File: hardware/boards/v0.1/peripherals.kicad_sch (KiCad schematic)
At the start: 7 parts, among them IC2 DA7280-00FVC, U21 LSM6DS3

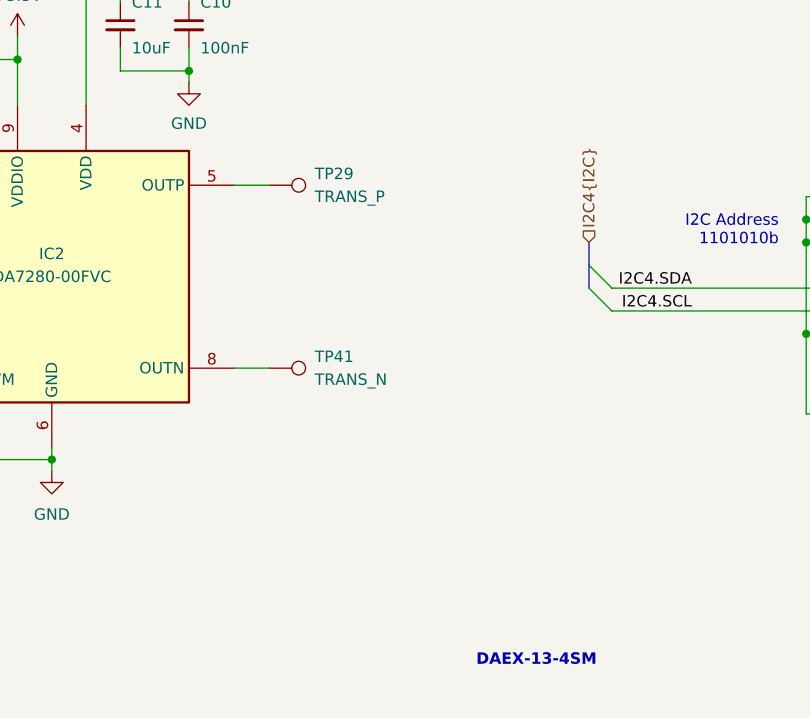
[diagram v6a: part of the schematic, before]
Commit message: feat: switch FM transmitter to I2S
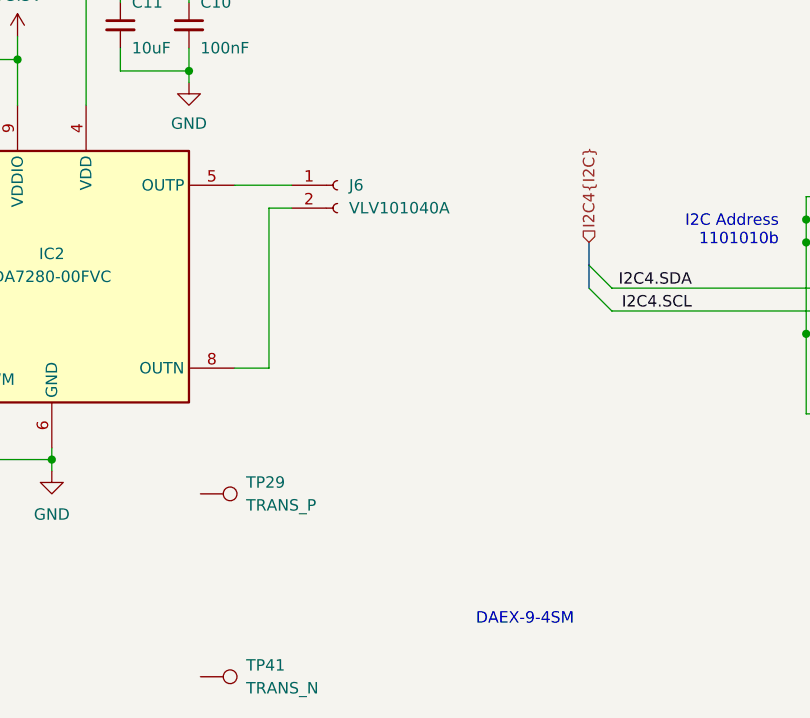
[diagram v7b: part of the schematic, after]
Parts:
- added J6: VLV101040A, pocket_synth:825-22-002-10-001101, symbol Connector:Conn_01x02_Socket
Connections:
- net at TP41.1: no longer IC2.8 (OUTN)
- net at IC2.5 (OUTP): now also J6.1 (Pin_1); no longer TP29.1
- new net: IC2.8 (OUTN), J6.2 (Pin_2)
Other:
- note added: "DAEX-9-4SM"
- note removed: "DAEX-13-4SM"
- moved on the sheet: TP29, TP41
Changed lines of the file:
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@@
 	(generator_version "9.0")
 	(paper "A4")
-	(text "DAEX-13-4SM"
+	(text "DAEX-9-4SM"
 		(exclude_from_sim no)
-		(at 116.078 103.632 0)
+		(at 114.808 99.06 0)
 		(effects
 			(font
 				(size 1.27 1.27)
-				(thickness 0.254)
-				(bold yes)
 			)
 		)
@@
 	(wire
 		(pts
+			(xy 86.36 53.34) (xy 88.9 53.34)
+		)
+		(stroke
+			(width 0)
+			(type default)
+		)
+	)
+	(wire
+		(pts
 			(xy 24.13 53.34) (xy 41.91 53.34)
 		)
@@
 	(wire
 		(pts
+			(xy 86.36 71.12) (xy 86.36 53.34)
+		)
+		(stroke
+			(width 0)
+			(type default)
+		)
+	)
+	(wire
+		(pts
 			(xy 147.32 64.77) (xy 124.46 64.77)
 		)
@@
 	(wire
 		(pts
-			(xy 82.55 50.8) (xy 86.36 50.8)
+			(xy 82.55 50.8) (xy 88.9 50.8)
 		)
 		(stroke
@@
 	(symbol
 		(lib_id "Connector:TestPoint")
-		(at 86.36 71.12 270)
+		(at 78.74 105.41 270)
 		(unit 1)
 		(exclude_from_sim no)
@@
 		(fields_autoplaced yes)
 		(property "Reference" "TP41"
-			(at 91.44 69.8499 90)
+			(at 83.82 104.1399 90)
 			(effects
 				(font
@@
 		)
 		(property "Value" "TRANS_N"
-			(at 91.44 72.3899 90)
+			(at 83.82 106.6799 90)
 			(effects
 				(font
@@
 		)
 		(property "Footprint" "TestPoint:TestPoint_Pad_D2.5mm"
-			(at 86.36 76.2 0)
+			(at 78.74 110.49 0)
 			(effects
 				(font
@@
 		)
 		(property "Datasheet" "~"
-			(at 86.36 76.2 0)
+			(at 78.74 110.49 0)
 			(effects
 				(font
@@
 		)
 		(property "Description" "test point"
-			(at 86.36 71.12 0)
+			(at 78.74 105.41 0)
 			(effects
 				(font
@@
 	)
 	(symbol
+		(lib_id "Connector:Conn_01x02_Socket")
+		(at 93.98 50.8 0)
+		(unit 1)
+		(exclude_from_sim no)
+		(in_bom yes)
+		(on_board yes)
+		(dnp no)
+		(fields_autoplaced yes)
+		(property "Reference" "J6"
+			(at 95.25 50.7999 0)
+			(effects
+				(font
+					(size 1.27 1.27)
+				)
+				(justify left)
+			)
+		)
+		(property "Value" "VLV101040A"
+			(at 95.25 53.3399 0)
+			(effects
+				(font
+					(size 1.27 1.27)
+				)
+				(justify left)
+			)
+		)
+		(property "Footprint" "pocket_synth:825-22-002-10-001101"
+			(at 93.98 50.8 0)
+			(effects
+				(font
+					(size 1.27 1.27)
+				)
+				(hide yes)
+			)
+		)
+		(property "Datasheet" "~"
+			(at 93.98 50.8 0)
+			(effects
+				(font
+					(size 1.27 1.27)
+				)
+				(hide yes)
+			)
+		)
+		(property "Description" "Generic connector, single row, 01x02, script generated"
+			(at 93.98 50.8 0)
+			(effects
+				(font
+					(size 1.27 1.27)
+				)
+				(hide yes)
+			)
+		)
+		(pin "2"
+		)
+		(pin "1"
+		)
+		(instances
+			(project ""
+				(path "/485383b8-00f4-4405-b270-de249939cff4/f91e71c7-727a-4ef4-a387-8ca9d7b49c20"
+					(reference "J6")
+					(unit 1)
+				)
+			)
+		)
+	)
+	(symbol
 		(lib_id "Connector:TestPoint")
-		(at 86.36 50.8 270)
+		(at 78.74 85.09 270)
 		(unit 1)
 		(exclude_from_sim no)
@@
 		(fields_autoplaced yes)
 		(property "Reference" "TP29"
-			(at 91.44 49.5299 90)
+			(at 83.82 83.8199 90)
 			(effects
 				(font
@@
 		)
 		(property "Value" "TRANS_P"
-			(at 91.44 52.0699 90)
+			(at 83.82 86.3599 90)
 			(effects
 				(font
@@
 		)
 		(property "Footprint" "TestPoint:TestPoint_Pad_D2.5mm"
-			(at 86.36 55.88 0)
+			(at 78.74 90.17 0)
 			(effects
 				(font
@@
 		)
 		(property "Datasheet" "~"
-			(at 86.36 55.88 0)
+			(at 78.74 90.17 0)
 			(effects
 				(font
@@
 		)
 		(property "Description" "test point"
-			(at 86.36 50.8 0)
-			(effects
-				(font
+			(at 78.74 85.09 0)
+			(effects
+				(font

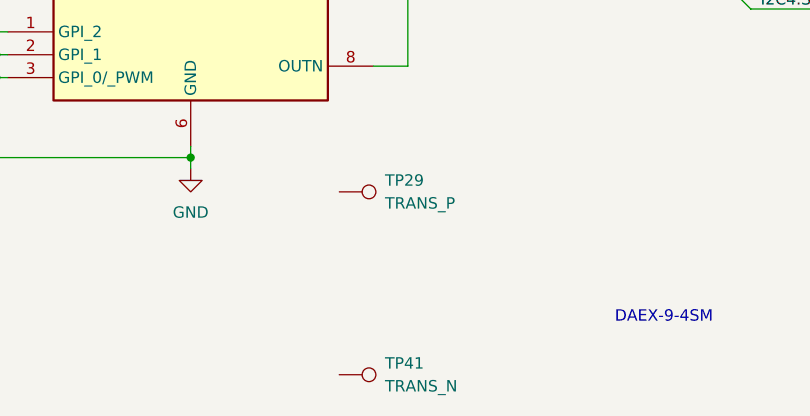
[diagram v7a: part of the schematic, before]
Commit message: feat: add FM reset pins, add fiducials
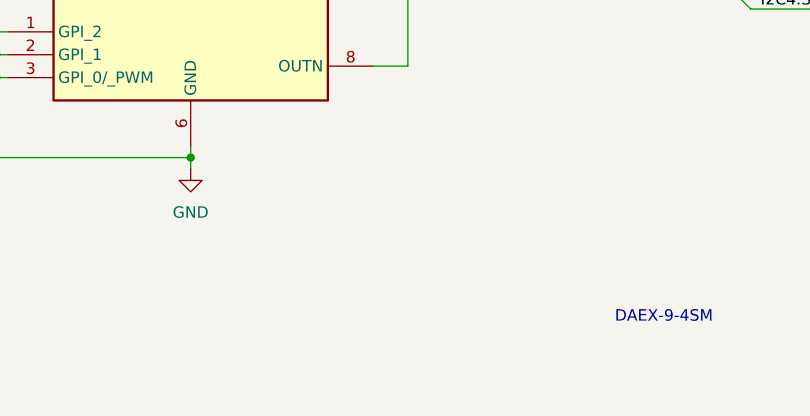
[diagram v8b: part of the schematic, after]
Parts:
- removed TP29: TRANS_P, TestPoint:TestPoint_Pad_D2.5mm, symbol Connector:TestPoint
- removed TP41: TRANS_N, TestPoint:TestPoint_Pad_D2.5mm, symbol Connector:TestPoint
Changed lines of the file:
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@@
-	)
-	(symbol
-		(lib_id "Connector:TestPoint")
-		(at 78.74 105.41 270)
-		(unit 1)
-		(exclude_from_sim no)
-		(in_bom yes)
-		(on_board yes)
-		(dnp no)
-		(fields_autoplaced yes)
-		(property "Reference" "TP41"
-			(at 83.82 104.1399 90)
-			(effects
-				(font
-					(size 1.27 1.27)
-				)
-				(justify left)
-			)
-		)
-		(property "Value" "TRANS_N"
-			(at 83.82 106.6799 90)
-			(effects
-				(font
-					(size 1.27 1.27)
-				)
-				(justify left)
-			)
-		)
-		(property "Footprint" "TestPoint:TestPoint_Pad_D2.5mm"
-			(at 78.74 110.49 0)
-			(effects
-				(font
-					(size 1.27 1.27)
-				)
-				(hide yes)
-			)
-		)
-		(property "Datasheet" "~"
-			(at 78.74 110.49 0)
-			(effects
-				(font
-					(size 1.27 1.27)
-				)
-				(hide yes)
-			)
-		)
-		(property "Description" "test point"
-			(at 78.74 105.41 0)
-			(effects
-				(font
-					(size 1.27 1.27)
-				)
-				(hide yes)
-			)
-		)
-		(pin "1"
-		)
-		(instances
-			(project "pocket_synth"
-				(path "/485383b8-00f4-4405-b270-de249939cff4/f91e71c7-727a-4ef4-a387-8ca9d7b49c20"
-					(reference "TP41")
-					(unit 1)
-				)
-			)
-		)
 	)
 	(symbol
@@
 					(unit 1)
 				)
-			)
-		)
-	)
-	(symbol
-		(lib_id "Connector:TestPoint")
-		(at 78.74 85.09 270)
-		(unit 1)
-		(exclude_from_sim no)
-		(in_bom yes)
-		(on_board yes)
-		(dnp no)
-		(fields_autoplaced yes)
-		(property "Reference" "TP29"
-			(at 83.82 83.8199 90)
-			(effects
-				(font
-					(size 1.27 1.27)
-				)
-				(justify left)
-			)
-		)
-		(property "Value" "TRANS_P"
-			(at 83.82 86.3599 90)
-			(effects
-				(font
-					(size 1.27 1.27)
-				)
-				(justify left)
-			)
-		)
-		(property "Footprint" "TestPoint:TestPoint_Pad_D2.5mm"
-			(at 78.74 90.17 0)
-			(effects
-				(font
-					(size 1.27 1.27)
-				)
-				(hide yes)
-			)
-		)
-		(property "Datasheet" "~"
-			(at 78.74 90.17 0)
-			(effects
-				(font
-					(size 1.27 1.27)
-				)
-				(hide yes)
-			)
-		)
-		(property "Description" "test point"
-			(at 78.74 85.09 0)
-			(effects
-				(font
-					(size 1.27 1.27)
-				)
-				(hide yes)
-			)
-		)
-		(pin "1"
-		)
-		(instances
-			(project ""
-				(path "/485383b8-00f4-4405-b270-de249939cff4/f91e71c7-727a-4ef4-a387-8ca9d7b49c20"
-					(reference "TP29")
-					(unit 1)
-				)
